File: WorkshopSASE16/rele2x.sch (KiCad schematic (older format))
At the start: 15 parts, among them J1 TB_1X3, J2 TB_1X3, K1 RELAY_C, K2 RELAY_C, Q1 2N2222, Q2 2N2222

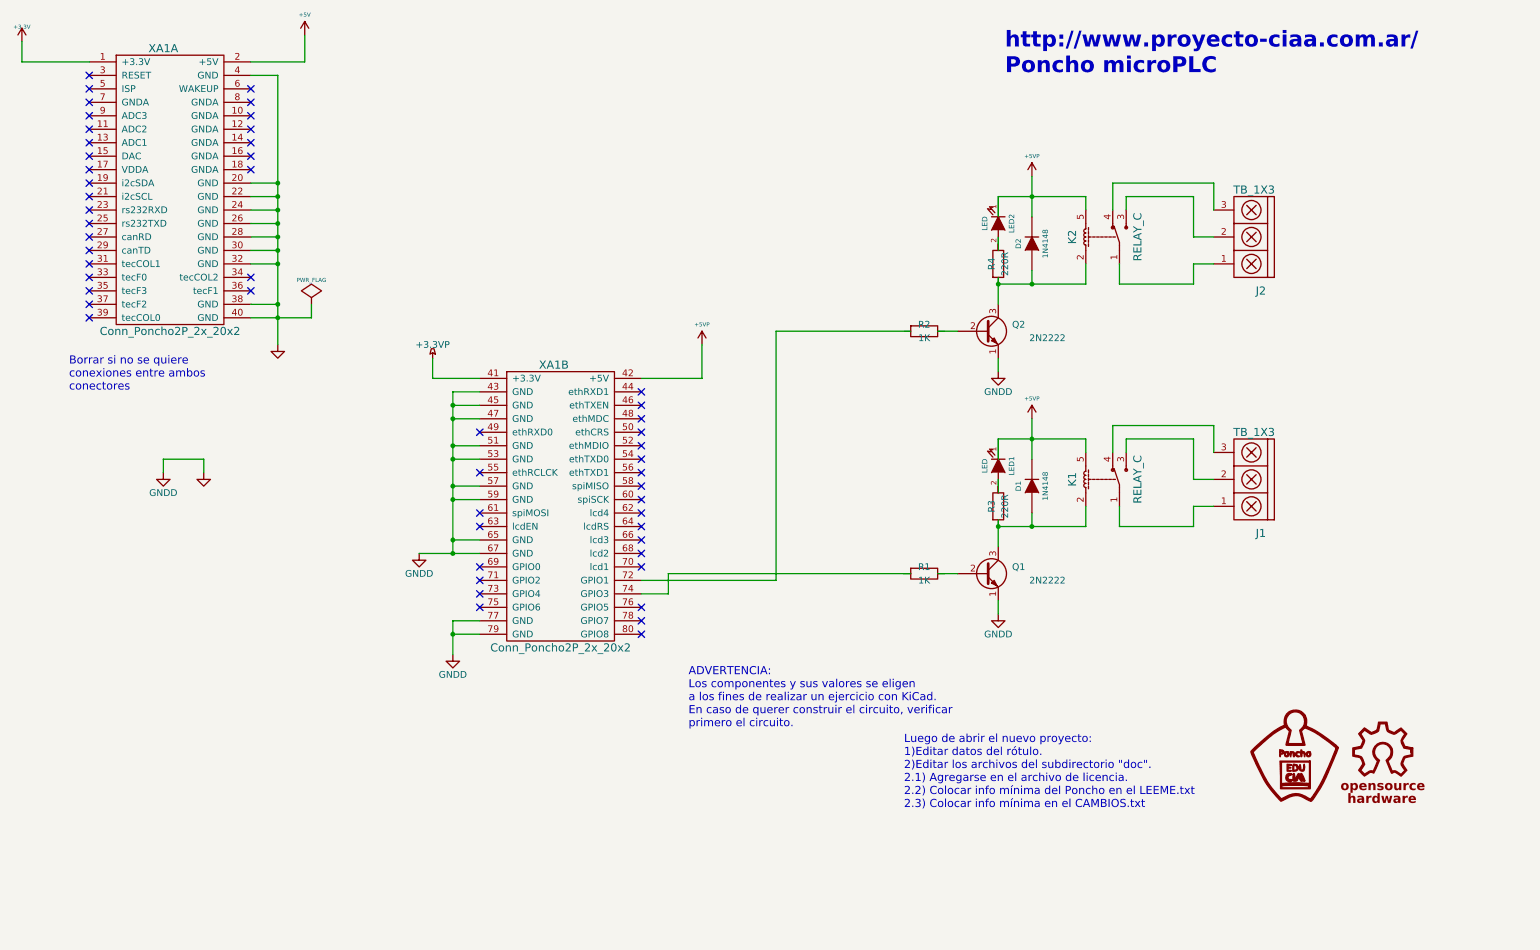
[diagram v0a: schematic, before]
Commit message: Agrego campos para KiCost.
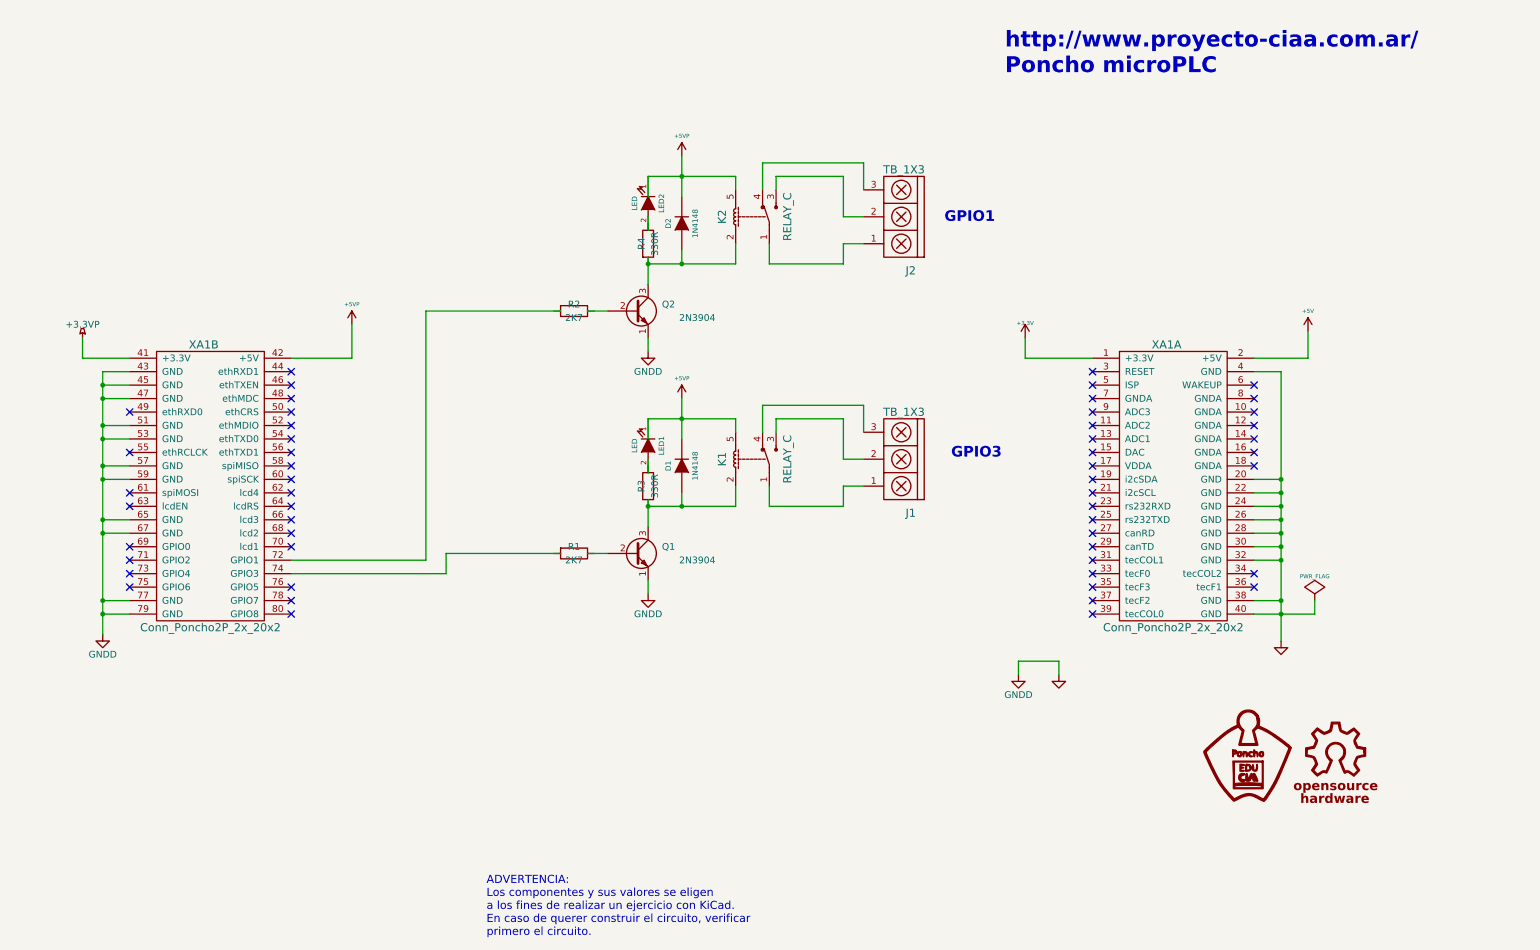
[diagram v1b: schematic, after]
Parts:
- D1, D2: Digikey# (none) -> 1N4148FSTR-ND; Manf (none) -> Fairchild; Manf# (none) -> 1N4148TR
- J1, J2: Digikey# (none) -> 796949-3-ND; Manf (none) -> TE; Manf# (none) -> 796949-3
- K1, K2: Digikey# (none) -> PB1321-ND; Manf (none) -> TE; Manf# (none) -> ORWH-SH-112D,N000
- LED1, LED2: Digikey# (none) -> 1125-1182-ND; Manf (none) -> Marktech; Manf# (none) -> MT1403-RG-A
- Q1, Q2: value 2N2222 -> 2N3904; Digikey# (none) -> 2N3904-APTB-ND; Manf (none) -> Micro; Manf# (none) -> 2N3904-AP
- R1, R2: value 1K -> 2K7; Digikey# (none) -> CF14JT2K70TR-ND; Manf (none) -> Stackpole; Manf# (none) -> CF14JT2K70
- R3, R4: value 220R -> 330R; Digikey# (none) -> CF14JT330RCT-ND; Manf (none) -> Stackpole; Manf# (none) -> CF14JT330R
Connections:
- wire segments 86 -> 85
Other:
- note added: "GPIO1"
- note added: "GPIO3"
- note removed: "Borrar si no se quiere \nconexiones entre ambos \nconectores"
- note removed: "Luego de abrir el nuevo proyecto:\n1)Editar datos del rótulo.\n2)Editar los archivos del subdirectorio "doc".\n2.1) Agregarse en el archivo de licencia.\n2.2) Colocar info mínima del Poncho en el LEEME.txt\n2.3) Colocar info mínima en el CAMBIOS.txt"
- moved on the sheet: D1, J1, K1, LED1, Q1, R1, R3, XA1A, XA1B

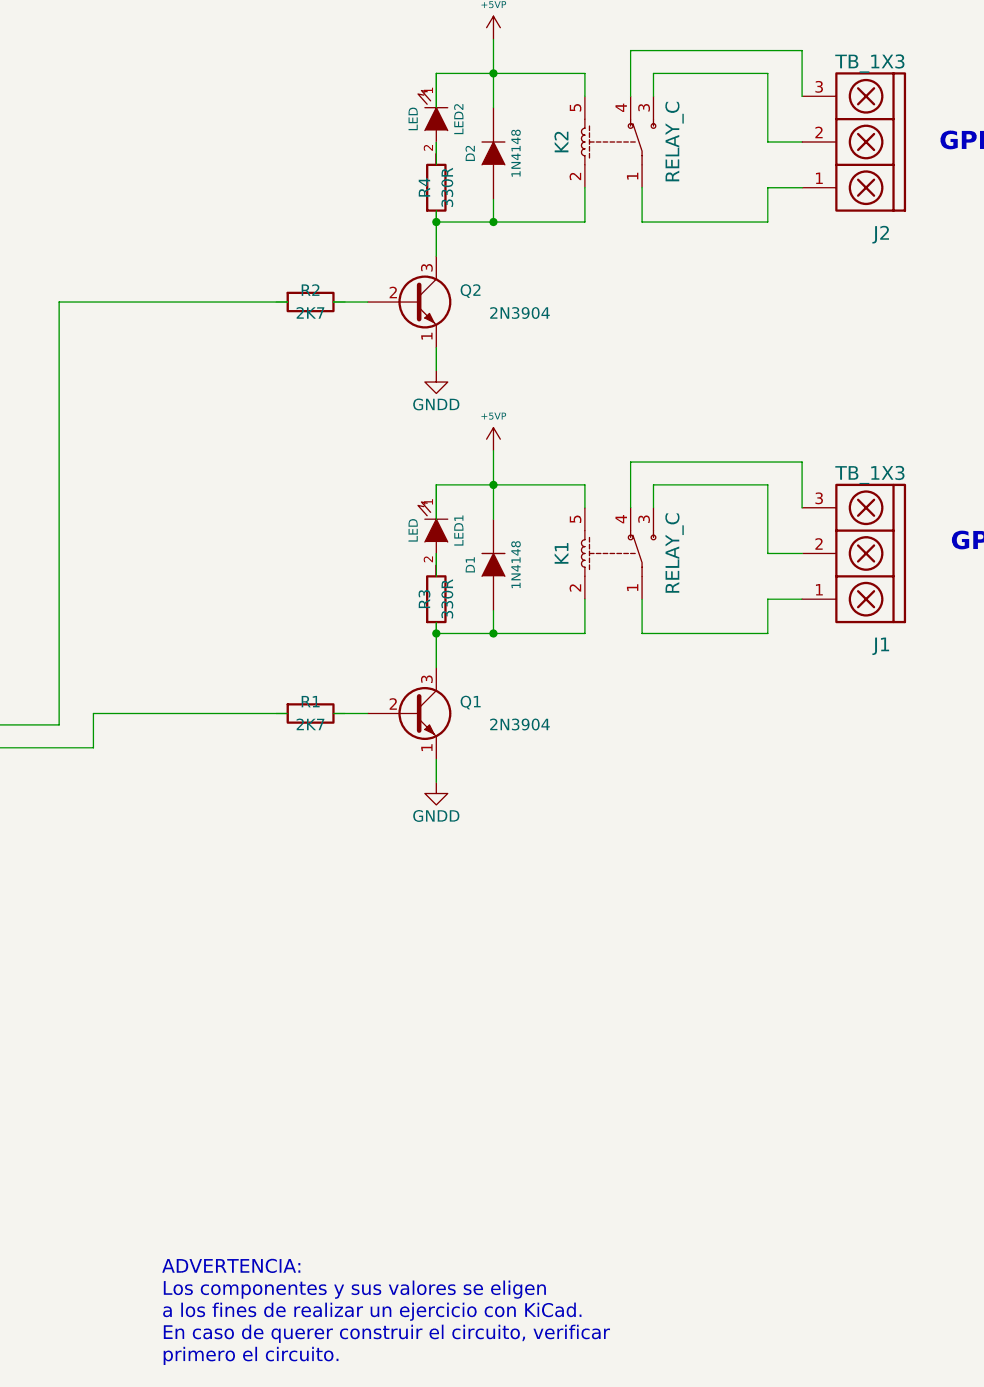
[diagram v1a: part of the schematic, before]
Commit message: Detalles al esquemático y al PCB.
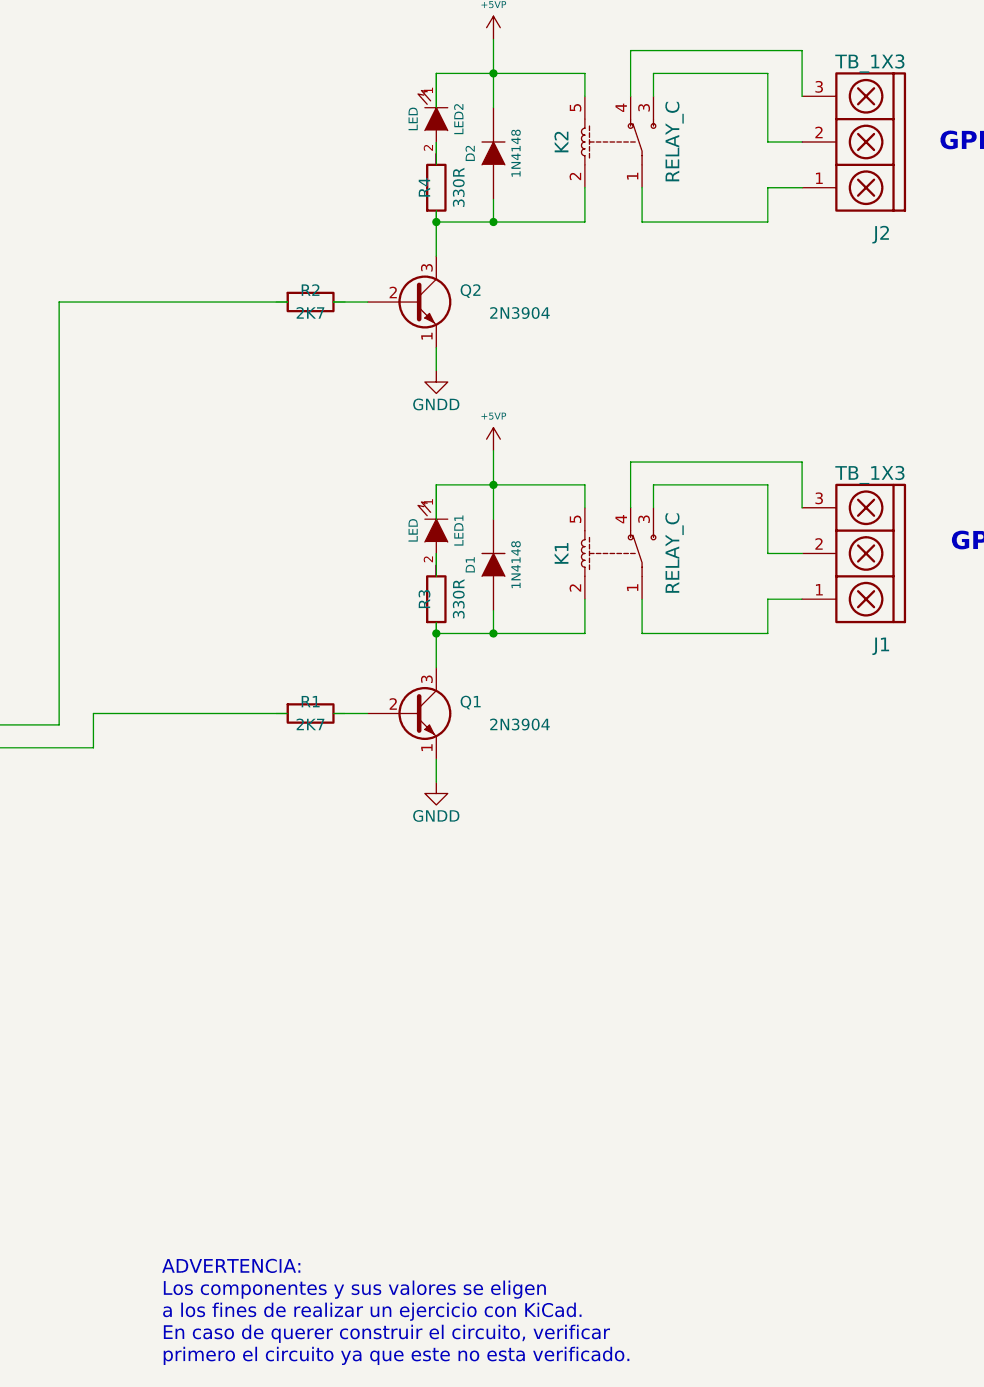
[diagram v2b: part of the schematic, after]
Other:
- note added: "ADVERTENCIA:\nLos componentes y sus valores se eligen\na los fines de realizar un ejercicio con KiCad.\nEn caso de querer construir el circuito, verificar \nprimero el circuito ya que este no esta verificado."
- note removed: "ADVERTENCIA:\nLos componentes y sus valores se eligen\na los fines de realizar un ejercicio con KiCad.\nEn caso de querer construir el circuito, verificar \nprimero el circuito."
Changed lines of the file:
@@
 P 5350 4000
 F 0 "R3" V 5300 4000 50  0000 C CNN
-F 1 "330R" V 5400 4000 50  0000 C CNN
+F 1 "330R" V 5450 4000 50  0000 C CNN
 F 2 "Resistors_ThroughHole:Resistor_Horizontal_RM10mm" H 5350 4000 60  0001 C CNN
 F 3 "" H 5350 4000 60  0000 C CNN
@@
 	5050 4500 4900 4500
 Text Notes 4150 7350 0    60   ~ 0
-ADVERTENCIA:\nLos componentes y sus valores se eligen\na los fines de realizar un ejercicio con KiCad.\nEn caso de querer construir el circuito, verificar \nprimero el circuito.
+ADVERTENCIA:\nLos componentes y sus valores se eligen\na los fines de realizar un ejercicio con KiCad.\nEn caso de querer construir el circuito, verificar \nprimero el circuito ya que este no esta verificado.
 NoConn ~ 1500 4450
 Wire Wire Line
@@
 P 5350 2200
 F 0 "R4" V 5300 2200 50  0000 C CNN
-F 1 "330R" V 5400 2200 50  0000 C CNN
+F 1 "330R" V 5450 2200 50  0000 C CNN
 F 2 "Resistors_ThroughHole:Resistor_Horizontal_RM10mm" H 5350 2200 60  0001 C CNN
 F 3 "" H 5350 2200 60  0000 C CNN
